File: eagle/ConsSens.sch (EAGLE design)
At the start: 6 parts

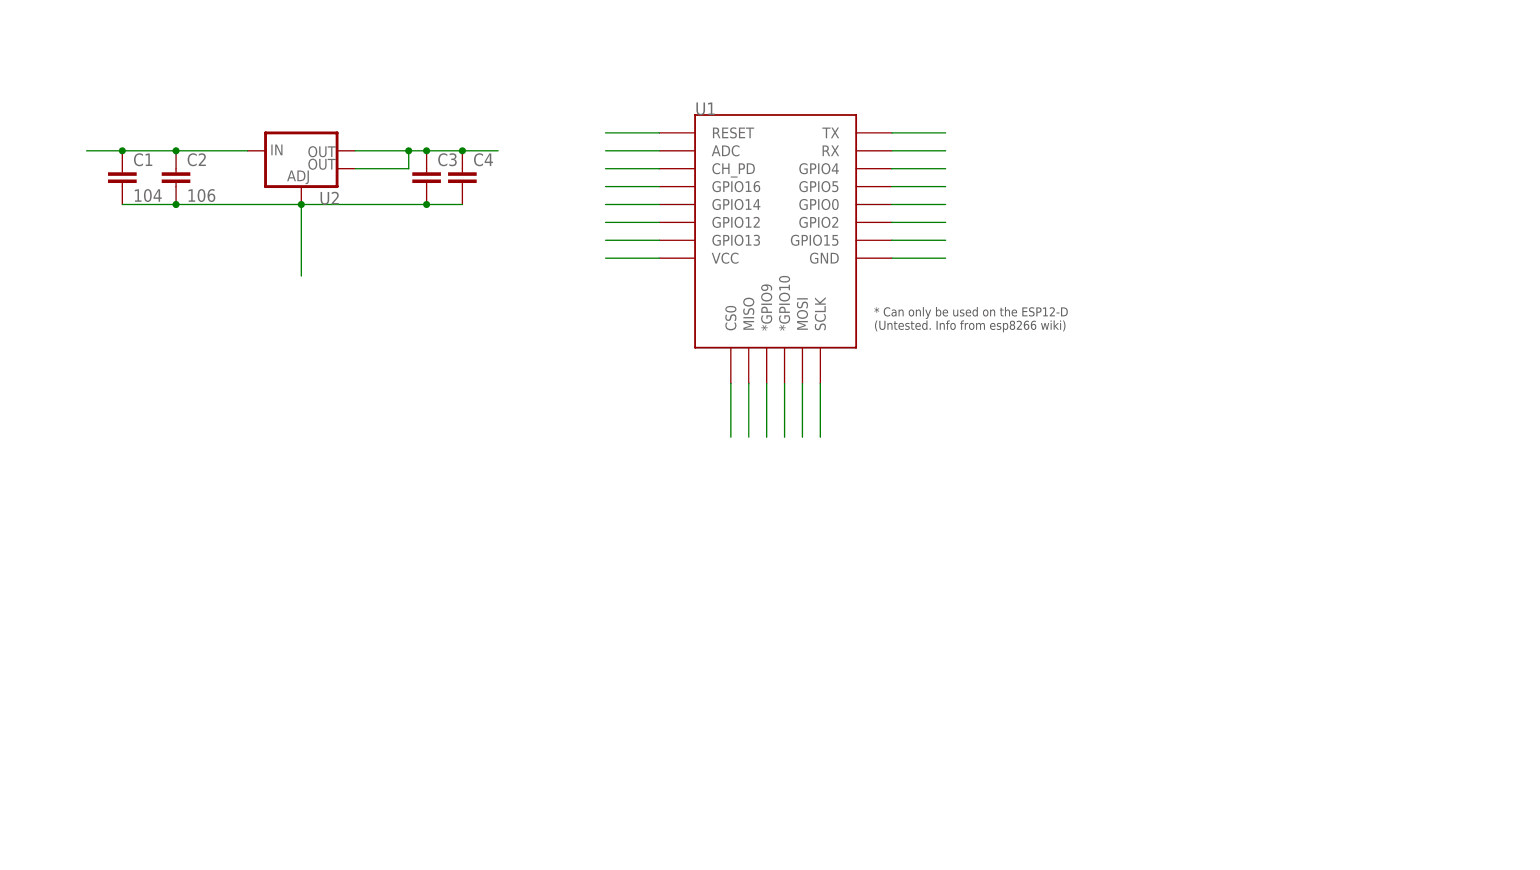
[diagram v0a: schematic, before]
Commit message: some new parts added to the layout, usb-serial eagle lib added
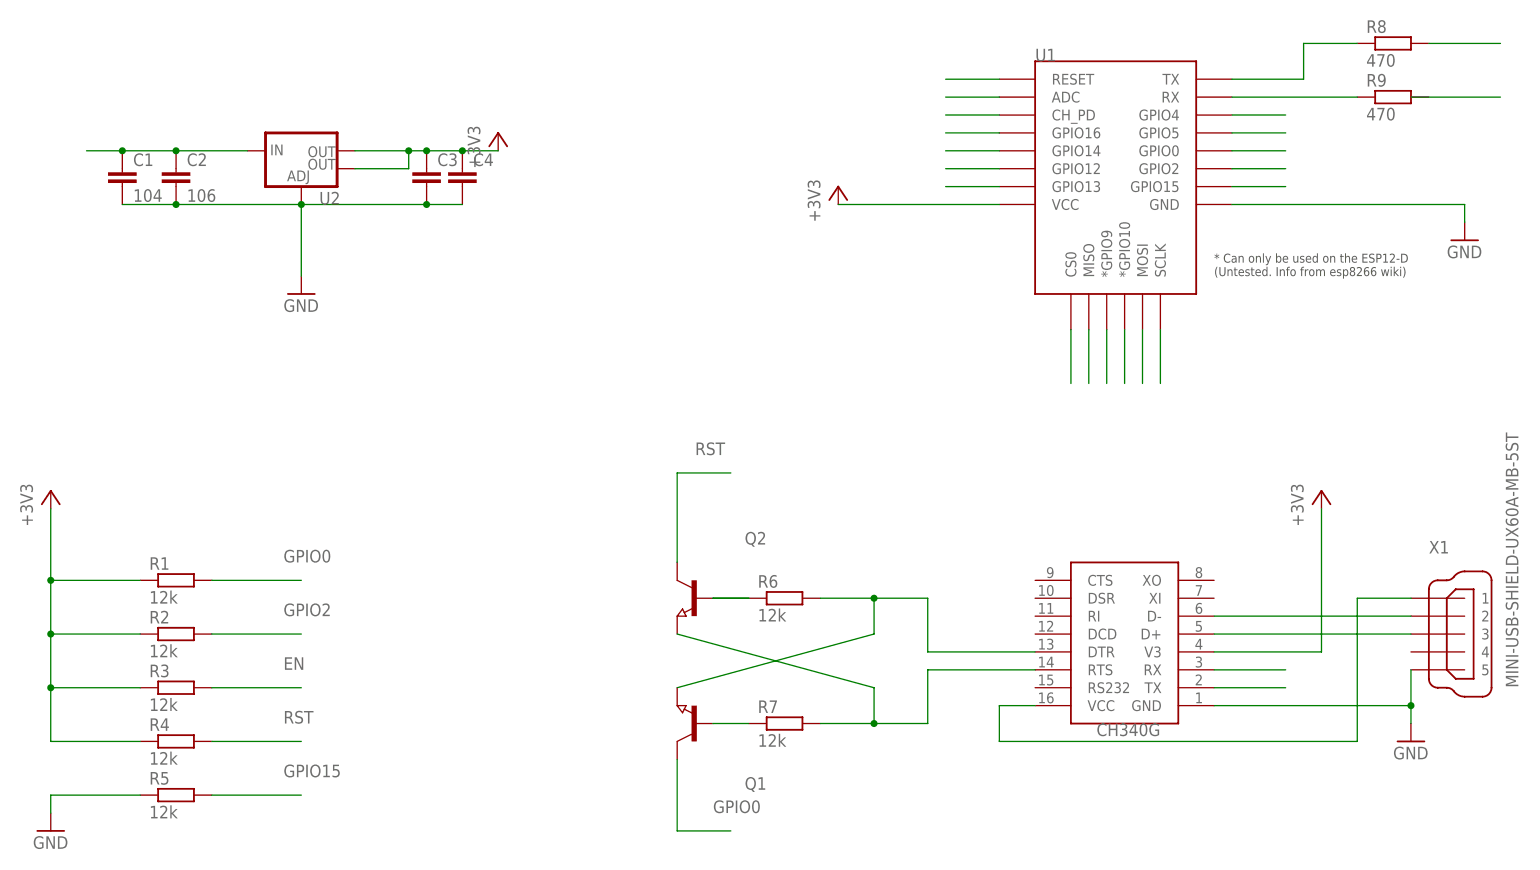
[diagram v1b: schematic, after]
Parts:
- added Q1, Q2: (no value), semicon-smd-ipc:NPN-TRANSISTOR_SOT23
- added R1, R2, R3, R4, R5, R6, R7: 12k, eagle-ltspice:RR0603
- added R8, R9: 470, eagle-ltspice:RR0603
- added U$1: CH340G, ch340g:CH340G
- added X1: MINI-USB-SHIELD-UX60A-MB-5ST, con-hirose:MINI-USB-SHIELD-UX60A-MB-5ST
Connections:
- new net +3V3: C3.1, C4.1, R1.1, R2.1, R3.1, R4.1, U$1.V3, U1.VCC, U2.OUT, U2.OUT@1
- new net 5V: U$1.VCC, X1G$1.1
- new net EN: R3.2
- new net N$1: Q1.B, R7.1
- new net N$15: U$1.RX
- new net N$16: U$1.TX
- new net N$2: Q2.B, R6.1
- new net N$3: Q2.E, R7.2, U$1.RTS
- new net N$4: Q1.E, R6.2, U$1.DTR
- new net N$5: U$1.D-, X1G$1.2
- new net N$6: U$1.D+, X1G$1.3
- new net N$7: R8.2
- net 3V3: no longer C3.1, C4.1, U1.VCC, U2.OUT, U2.OUT@1
- net GND: now also R5.1, U$1.GND, X1G$1.5
- net GPIO0: now also Q1.C, R1.2
- net GPIO15: now also R5.2
- net GPIO2: now also R2.2
- net RST: now also Q2.C, R4.2
- net RX: now also R9.1
- net TX: now also R8.1
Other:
- moved on the sheet: U1

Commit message: more layout added, also new eagle libs, and datasheets
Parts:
- removed U2: (no value), SparkFun-PowerIC:V_REG_LM1117SOT223
- added C5: 22pF, resistor:C-EUC0805
- added C6: 22pf, resistor:C-EUC0805
- added Q3: 12MHz, SparkFun-FreqCtrl:CRYSTALCRYSTAL-SMD-5X3-12MHZ
- added R10: 220k, eagle-ltspice:RR0603
- added R11: 100k, eagle-ltspice:RR0603
- added R12, R13, R14: 12k, eagle-ltspice:RR0603
- added U$2: LIPOCHARGER, aliexpress:LIPOCHARGER
- added U$3: MICROSD_SPI_MODE, con-molex-microsd:MICROSD_SPI_MODE
- added U3: 3.3V, SparkFun-PowerIC:V_REG_AP2112K-3.3V
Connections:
- net N$16 renamed RXD0
- removed net 3V3: U1.CH_PD
- removed net 5V: U$1.VCC, X1G$1.1
- removed net N$15: U$1.RX
- removed net N$7: R8.2
- removed net VIN: C1.1, C2.1, U2.IN
- new net N$20: U$3.RSV
- new net N$8: U$3.NC
- new net OUT+: C1.1, C2.1, R10.2, U$2.B+, U$2.OUT+, U3.IN
- new net TXD0: R8.2, U$1.RX
- new net USB5V: U$1.VCC, U$2.IN+, X1G$1.1
- new net XI: C6.1, Q3.2, U$1.XI
- new net XO: C5.1, Q3.1, U$1.XO
- net +3V3: now also U3.OUT; no longer U2.OUT, U2.OUT@1
- net ADC: now also R10.1, R11.2
- net EN: now also U1.CH_PD
- net GND: now also C5.2, C6.2, R11.1, R12.2, R13.2, R14.2, U$2.IN-, U$2.OUT-, U$3.VDD, U$3.VSS, U3.GND; no longer U2.ADJ
- net GPIO12: now also R14.1, U$3.DO
- net GPIO13: now also R12.1, U$3.DI
- net GPIO14: now also U$3.CLK
- net GPIO15: now also R13.1, U$3./CS
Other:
- moved on the sheet: C1, C2, C3, C4

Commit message: first routing
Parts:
- added 1-WIRE: (no value), con-lstb:MA03-1
- added I2C: (no value), con-lstb:MA04-1
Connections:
- new net GPO4: I2C.2
- net +3V3: now also 1-WIRE.1, I2C.1
- net GND: now also 1-WIRE.3, I2C.4
- net GPIO14: now also 1-WIRE.2
- net GPIO5: now also I2C.3
- net OUT+: now also U3.EN
- net RXD0: now also R9.2
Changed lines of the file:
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@@
 <part name="+3V5" library="supply1" deviceset="+3V3" device=""/>
 <part name="GND8" library="supply1" deviceset="GND" device=""/>
+<part name="I2C" library="con-lstb" deviceset="MA04-1" device=""/>
+<part name="1-WIRE" library="con-lstb" deviceset="MA03-1" device=""/>
 </parts>
 <sheets>
@@
 <instance part="+3V5" gate="G$1" x="35.56" y="-25.4"/>
 <instance part="GND8" gate="1" x="45.72" y="-60.96"/>
+<instance part="I2C" gate="1" x="60.96" y="111.76"/>
+<instance part="1-WIRE" gate="G$1" x="104.14" y="111.76"/>
 </instances>
 <busses>
@@
 <wire x1="7.62" y1="-53.34" x2="17.78" y2="-53.34" width="0.1524" layer="91"/>
 </segment>
+<segment>
+<pinref part="1-WIRE" gate="G$1" pin="2"/>
+<wire x1="111.76" y1="111.76" x2="124.46" y2="111.76" width="0.1524" layer="91"/>
+<label x="121.92" y="111.76" size="1.27" layer="95"/>
+</segment>
 </net>
 <net name="GPIO12" class="0">
@@
 <wire x1="142.24" y1="81.28" x2="149.86" y2="81.28" width="0.1524" layer="91"/>
 <label x="147.32" y="81.28" size="1.27" layer="95"/>
+</segment>
+<segment>
+<pinref part="I2C" gate="1" pin="3"/>
+<wire x1="68.58" y1="111.76" x2="78.74" y2="111.76" width="0.1524" layer="91"/>
+<label x="76.2" y="111.76" size="1.27" layer="95"/>
 </segment>
 </net>
@@
 <wire x1="45.72" y1="-55.88" x2="45.72" y2="-58.42" width="0.1524" layer="91"/>
 </segment>
+<segment>
+<pinref part="1-WIRE" gate="G$1" pin="3"/>
+<wire x1="111.76" y1="114.3" x2="124.46" y2="114.3" width="0.1524" layer="91"/>
+<label x="121.92" y="114.3" size="1.27" layer="95"/>
+</segment>
+<segment>
+<pinref part="I2C" gate="1" pin="4"/>
+<wire x1="68.58" y1="114.3" x2="78.74" y2="114.3" width="0.1524" layer="91"/>
+<label x="76.2" y="114.3" size="1.27" layer="95"/>
+</segment>
 </net>
 <net name="EN" class="0">
@@
 <junction x="33.02" y="86.36"/>
 </segment>
+<segment>
+<pinref part="1-WIRE" gate="G$1" pin="1"/>
+<wire x1="111.76" y1="109.22" x2="124.46" y2="109.22" width="0.1524" layer="91"/>
+<label x="121.92" y="109.22" size="1.27" layer="95"/>
+</segment>
+<segment>
+<wire x1="68.58" y1="106.68" x2="78.74" y2="106.68" width="0.1524" layer="91"/>
+<label x="76.2" y="106.68" size="1.27" layer="95"/>
+<pinref part="I2C" gate="1" pin="1"/>
+</segment>
 </net>
 <net name="N$1" class="0">
@@
 <net name="RXD0" class="0">
 <segment>
-<wire x1="167.64" y1="86.36" x2="180.34" y2="86.36" width="0.1524" layer="91"/>
+<wire x1="170.18" y1="86.36" x2="182.88" y2="86.36" width="0.1524" layer="91"/>
 <label x="177.8" y="86.36" size="1.27" layer="95"/>
+<pinref part="R9" gate="G$1" pin="2"/>
 </segment>
 <segment>
@@
 <segment>
 <pinref part="U3" gate="G$1" pin="IN"/>
-<wire x1="2.54" y1="86.36" x2="-7.62" y2="86.36" width="0.1524" layer="91"/>
+<wire x1="2.54" y1="86.36" x2="0" y2="86.36" width="0.1524" layer="91"/>
 <pinref part="C1" gate="G$1" pin="1"/>
+<wire x1="0" y1="86.36" x2="-7.62" y2="86.36" width="0.1524" layer="91"/>
 <wire x1="-7.62" y1="86.36" x2="-15.24" y2="86.36" width="0.1524" layer="91"/>
 <wire x1="-15.24" y1="86.36" x2="-40.64" y2="86.36" width="0.1524" layer="91"/>
@@
 <wire x1="-40.64" y1="81.28" x2="-40.64" y2="86.36" width="0.1524" layer="91"/>
 <junction x="-40.64" y="86.36"/>
+<pinref part="U3" gate="G$1" pin="EN"/>
+<wire x1="2.54" y1="81.28" x2="0" y2="81.28" width="0.1524" layer="91"/>
+<wire x1="0" y1="81.28" x2="0" y2="86.36" width="0.1524" layer="91"/>
+<junction x="0" y="86.36"/>
 </segment>
 </net>
@@
 <wire x1="132.08" y1="-60.96" x2="132.08" y2="-50.8" width="0.1524" layer="91"/>
 <junction x="132.08" y="-60.96"/>
+<label x="132.08" y="-50.8" size="1.27" layer="95"/>
 </segment>
 <segment>
 <pinref part="U$1" gate="G$1" pin="XI"/>
 <wire x1="139.7" y1="15.24" x2="144.78" y2="15.24" width="0.1524" layer="91"/>
+<label x="144.78" y="15.24" size="1.27" layer="95"/>
 </segment>
 </net>
@@
 <wire x1="106.68" y1="-60.96" x2="106.68" y2="-50.8" width="0.1524" layer="91"/>
 <junction x="106.68" y="-60.96"/>
+<label x="106.68" y="-50.8" size="1.27" layer="95"/>
 </segment>
 <segment>
 <pinref part="U$1" gate="G$1" pin="XO"/>
 <wire x1="139.7" y1="17.78" x2="144.78" y2="17.78" width="0.1524" layer="91"/>
+<label x="144.78" y="17.78" size="1.27" layer="95"/>
 </segment>
 </net>
@@
 </segment>
 </net>
+<net name="GPO4" class="0">
+<segment>
+<pinref part="I2C" gate="1" pin="2"/>
+<wire x1="68.58" y1="109.22" x2="78.74" y2="109.22" width="0.1524" layer="91"/>
+<label x="76.2" y="109.22" size="1.27" layer="95"/>
+</segment>
+</net>
